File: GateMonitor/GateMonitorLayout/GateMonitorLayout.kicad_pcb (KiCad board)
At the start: 2 copper layers, 100 x 50 mm, 25 parts, among them J1 Screw_Terminal_01x03, J2 PIR sensor, J3 Conn_01x03, J4 Hall effect, Q1 IRLB8721PBF, U1 Ra01_Breakout_Module, U2 MIC2954, U3 PICAXE-14M2

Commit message: Gate monitor layout mostly done
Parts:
- removed F1: 250mA, Custom:Fuseholder5x20_horiz_open_lateral_Type-II
- added J5: Hall effect, TerminalBlock:TerminalBlock_Altech_AK300-3_P5.00mm, F.Cu at (188.0, 97.7)
- added R10: LDR07, OptoDevice:R_LDR_7x6mm_P5.1mm_Vertical, F.Cu at (172.7, 77.4)
- added R11: 4.7k, Resistor_THT:R_Axial_DIN0207_L6.3mm_D2.5mm_P7.62mm_Horizontal, F.Cu at (172.7, 87.5)
- C1: footprint Capacitor_THT:CP_Radial_D6.3mm_P2.50mm -> Capacitor_THT:C_Rect_L13.0mm_W6.0mm_P10.00mm_FKS3_FKP3_MKS4
- C2: footprint Capacitor_THT:C_Disc_D3.0mm_W1.6mm_P2.50mm -> Capacitor_THT:C_Disc_D7.0mm_W2.5mm_P5.00mm
- C3: value 100n -> 3.3u; footprint Capacitor_THT:C_Disc_D3.0mm_W1.6mm_P2.50mm -> Capacitor_THT:CP_Radial_D8.0mm_P5.00mm
- C4: value 3.3u -> 100n; footprint Capacitor_THT:CP_Radial_D6.3mm_P2.50mm -> Capacitor_THT:C_Axial_L3.8mm_D2.6mm_P12.50mm_Horizontal
- D1, D2: footprint Diode_THT:D_DO-41_SOD81_P10.16mm_Horizontal -> Diode_THT:D_DO-41_SOD81_P5.08mm_Vertical_AnodeUp
- J2: value PIR sensor -> Conn_01x03; footprint Connector_PinHeader_2.54mm:PinHeader_1x03_P2.54mm_Vertical -> Connector_Molex:Molex_KK-254_AE-6410-03A_1x03_P2.54mm_Vertical
- J3: value Conn_01x03 -> PIR sensor; footprint Connector_Molex:Molex_KK-254_AE-6410-03A_1x03_P2.54mm_Vertical -> Connector_PinHeader_2.54mm:PinHeader_1x03_P2.54mm_Vertical
- J4: value Hall effect -> AHT20 temperature sensor; footprint TerminalBlock:TerminalBlock_Altech_AK300-3_P5.00mm -> Connector_PinSocket_2.54mm:PinSocket_1x04_P2.54mm_Vertical
- R1: value 22k -> 10k
- R2: value 330k -> 22k; footprint Resistor_THT:R_Axial_DIN0207_L6.3mm_D2.5mm_P10.16mm_Horizontal -> Resistor_THT:R_Axial_DIN0207_L6.3mm_D2.5mm_P5.08mm_Vertical
- R3: value 220k -> 330k; footprint Resistor_THT:R_Axial_DIN0207_L6.3mm_D2.5mm_P10.16mm_Horizontal -> Resistor_THT:R_Axial_DIN0207_L6.3mm_D2.5mm_P5.08mm_Vertical
- R4: value 10k -> 220k
- R6: value 4.7k -> 33k; footprint Resistor_THT:R_Axial_DIN0207_L6.3mm_D2.5mm_P10.16mm_Horizontal -> Resistor_THT:R_Axial_DIN0207_L6.3mm_D2.5mm_P5.08mm_Vertical
- R7: value LDR07 -> 4.7k; footprint OptoDevice:R_LDR_5.1x4.3mm_P3.4mm_Vertical -> Resistor_THT:R_Axial_DIN0204_L3.6mm_D1.6mm_P2.54mm_Vertical
- R8: value 33k -> 4.7k; footprint Resistor_THT:R_Axial_DIN0207_L6.3mm_D2.5mm_P10.16mm_Horizontal -> Resistor_THT:R_Axial_DIN0207_L6.3mm_D2.5mm_P5.08mm_Vertical
- U2: value MIC2954 -> PICAXE-18M2; footprint Package_DIP:DIP-8_W7.62mm_Socket_LongPads -> Package_DIP:DIP-18_W7.62mm_Socket_LongPads
- U3: value PICAXE-14M2 -> MIC2954; footprint Package_DIP:DIP-14_W7.62mm_Socket_LongPads -> Package_DIP:DIP-8_W7.62mm_Socket_LongPads
- moved C3 98.0 mm to (92.7, 102.8), turned to 90 degrees
- moved R6 78.2 mm to (104.1, 77.4), turned to 90 degrees
- moved R4 77.9 mm to (104.1, 97.7), turned to 90 degrees
- moved U3 66.5 mm to (119.4, 100.2), turned to 180 degrees
- moved J2 66.2 mm to (129.5, 74.8), turned to -90 degrees
- moved C2 56.4 mm to (101.6, 102.8), turned to 90 degrees
- moved R7 56.3 mm to (147.3, 77.4), turned to 90 degrees
- moved C4 44.1 mm to (124.5, 87.7), turned to -90 degrees
- moved R8 40.6 mm to (170.2, 87.5)
- moved R3 38.1 mm to (109.2, 102.8), turned to 90 degrees
- moved R1 37.3 mm to (137.2, 77.4)
- moved D1 36.6 mm to (101.6, 77.4)
- moved R5 33.0 mm to (162.6, 82.5)
- moved D2 27.8 mm to (111.8, 77.4), turned to 180 degrees
- moved D3 26.9 mm to (166.4, 74.8), turned to 90 degrees
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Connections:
- C2 pad 2: Net-(U2-FB) -> Net-(U3-FB)
- C3 pad 1: GNDREF -> +3.3V
- C3 pad 2: +3.3V -> GNDREF
- C4 pad 1: +3.3V -> GNDREF
- C4 pad 2: GNDREF -> +3.3V
- D1 pad 1: Net-(D1-K) -> +BATT
- J1 pad 1: GNDREF -> +BATT
- J1 pad 3: Net-(D1-K) -> GNDREF
- J2 pad 1: +3.3V -> GNDREF
- J2 pad 3: GNDREF -> Net-(J2-Pin_3)
- J3 pad 1: GNDREF -> +3.3V
- J3 pad 2: Net-(J3-Pin_2) -> /PIR
- J3 pad 3: Net-(J3-Pin_3) -> GNDREF
- J4 pad 1: +BATT -> +3.3V
- J4 pad 2: Net-(J4-Pin_2) -> GNDREF
- J4 pad 3: GNDREF -> /I2C SCL
- Q1 pad 1: Net-(Q1-G) -> /Aux power
- R1 pad 1: Net-(J3-Pin_2) -> Net-(J2-Pin_2)
- R1 pad 2: Net-(J2-Pin_2) -> GNDREF
- R2 pad 1: +3.3V -> Net-(U2-C.4/RX)
- R2 pad 2: Net-(U2-FB) -> Net-(J2-Pin_2)
- R3 pad 1: Net-(U2-FB) -> +3.3V
- R3 pad 2: GNDREF -> Net-(U3-FB)
- R4 pad 1: Net-(J3-Pin_2) -> Net-(U3-FB)
- R5 pad 1: Net-(J3-Pin_3) -> /LED
- R6 pad 1: +3.3V -> +BATT
- R6 pad 2: Net-(U3-B.3) -> /Battery ADC
- R7 pad 1: Net-(U3-B.3) -> /Battery ADC
- R8 pad 1: +BATT -> +3.3V
- R8 pad 2: Net-(U3-B.2) -> /I2C SCL
- R9 pad 1: Net-(U3-B.2) -> +3.3V
- R9 pad 2: GNDREF -> /LDR ADC
- U2 pad 1: +3.3V -> /Battery ADC
- U2 pad 2: unconnected-(U2-SNS-Pad2) -> Net-(J2-Pin_3)
- U2 pad 3: unconnected-(U2-SHDN-Pad3) -> Net-(U2-C.4/RX)
- U2 pad 4: GNDREF -> Net-(U1-DIO0)
- U2 pad 5: unconnected-(U2-/ERR-Pad5) -> GNDREF
- U2 pad 6: unconnected-(U2-TAP-Pad6) -> Net-(U1-MOSI)
- U2 pad 7: Net-(U2-FB) -> /I2C SDA
- U2 pad 8: Net-(D2-K) -> Net-(U1-SCK)
- U3 pad 2: Net-(J2-Pin_2) -> unconnected-(U3-SNS-Pad2)
- U3 pad 3: Net-(U1-RST) -> unconnected-(U3-SHDN-Pad3)
- U3 pad 4: Net-(U1-MISO) -> GNDREF
- U3 pad 5: Net-(U1-MOSI) -> unconnected-(U3-/ERR-Pad5)
- U3 pad 6: Net-(U1-SCK) -> unconnected-(U3-TAP-Pad6)
- U3 pad 7: Net-(U1-NSS) -> Net-(U3-FB)
- U3 pad 8: Net-(U1-DIO0) -> Net-(D2-K)
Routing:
- net Net-(Q1-G): track 146.1 -> 0.00 mm, vias 4 -> 0
- net /Aux power: track 0.00 -> 108.1 mm, vias 0 -> 4
- net /I2C SDA: track 0.00 -> 66.0 mm, vias 0 -> 4
- net Net-(U1-RST): track 71.3 -> 12.7 mm, vias 4 -> 0
- net Net-(U3-B.2): track 58.0 -> 0.00 mm, vias 4 -> 0
- net /Battery ADC: track 0.00 -> 50.8 mm, vias 0 -> 2
- net Net-(J4-Pin_2): track 46.5 -> 0.00 mm, vias 4 -> 0
- net /Hall effect: track 0.00 -> 44.0 mm, vias 0 -> 2
- net Net-(U1-SCK): track 56.6 -> 12.7 mm, vias 4 -> 0
- net Net-(D1-K): track 43.2 -> 0.00 mm, vias 4 -> 0
- net Net-(U1-NSS): track 27.9 -> 62.5 mm, vias 2 -> 4
- net Net-(D1-A): track 43.3 -> 11.8 mm, vias 3 -> 0
- net +BATT: track 40.6 -> 12.8 mm, vias 4 -> 0
- net Net-(D3-A): track 30.5 -> 3.81 mm, vias 2 -> 0
- net /I2C SCL: track 0.00 -> 22.9 mm, vias 0 -> 2
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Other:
- board size 100 x 50 mm -> 113 x 44.5 mm

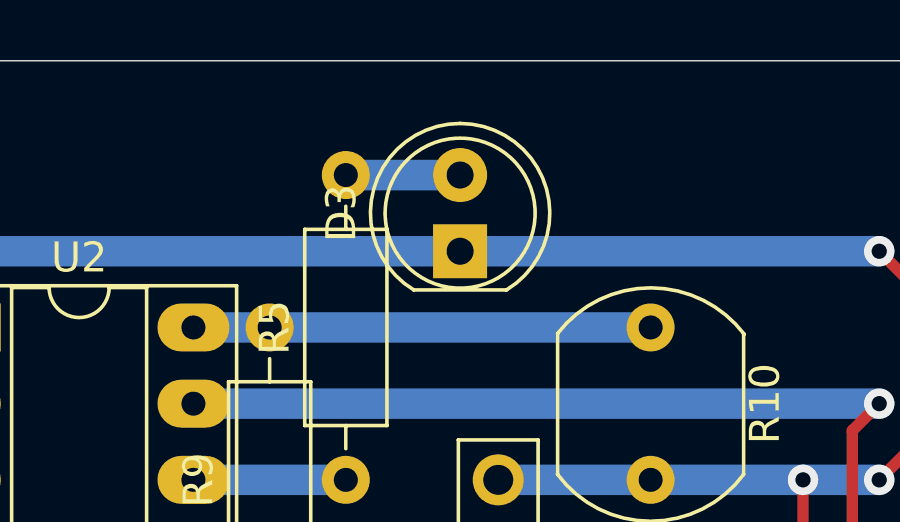
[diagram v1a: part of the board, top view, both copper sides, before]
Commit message: Added holes and grid to gate monitor layout
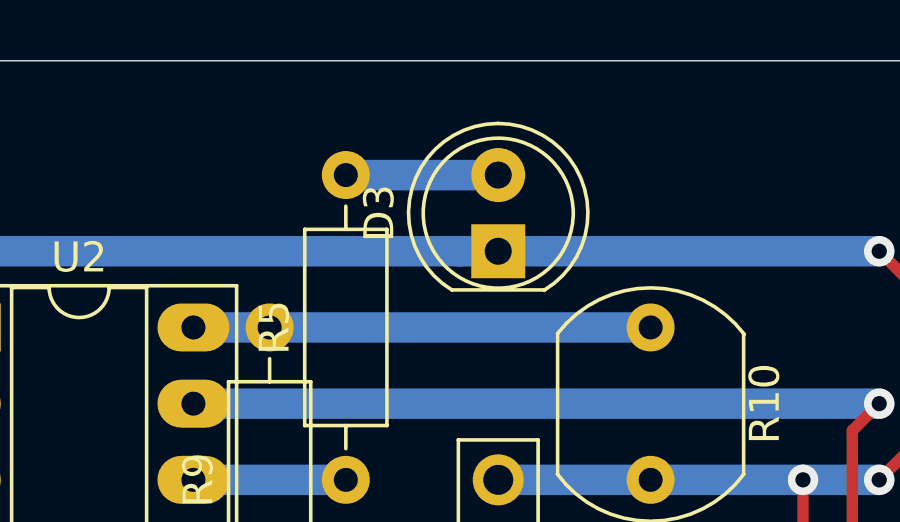
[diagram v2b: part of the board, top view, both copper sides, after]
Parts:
- R3: value 330k -> 470k
- R4: value 220k -> 270k
- moved D3 1.27 mm to (167.6, 74.8)
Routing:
- net Net-(D3-A): track 3.81 -> 5.08 mm
